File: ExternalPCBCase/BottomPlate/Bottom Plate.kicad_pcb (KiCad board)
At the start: 2 copper layers, 150 x 104.9 mm, 9 parts

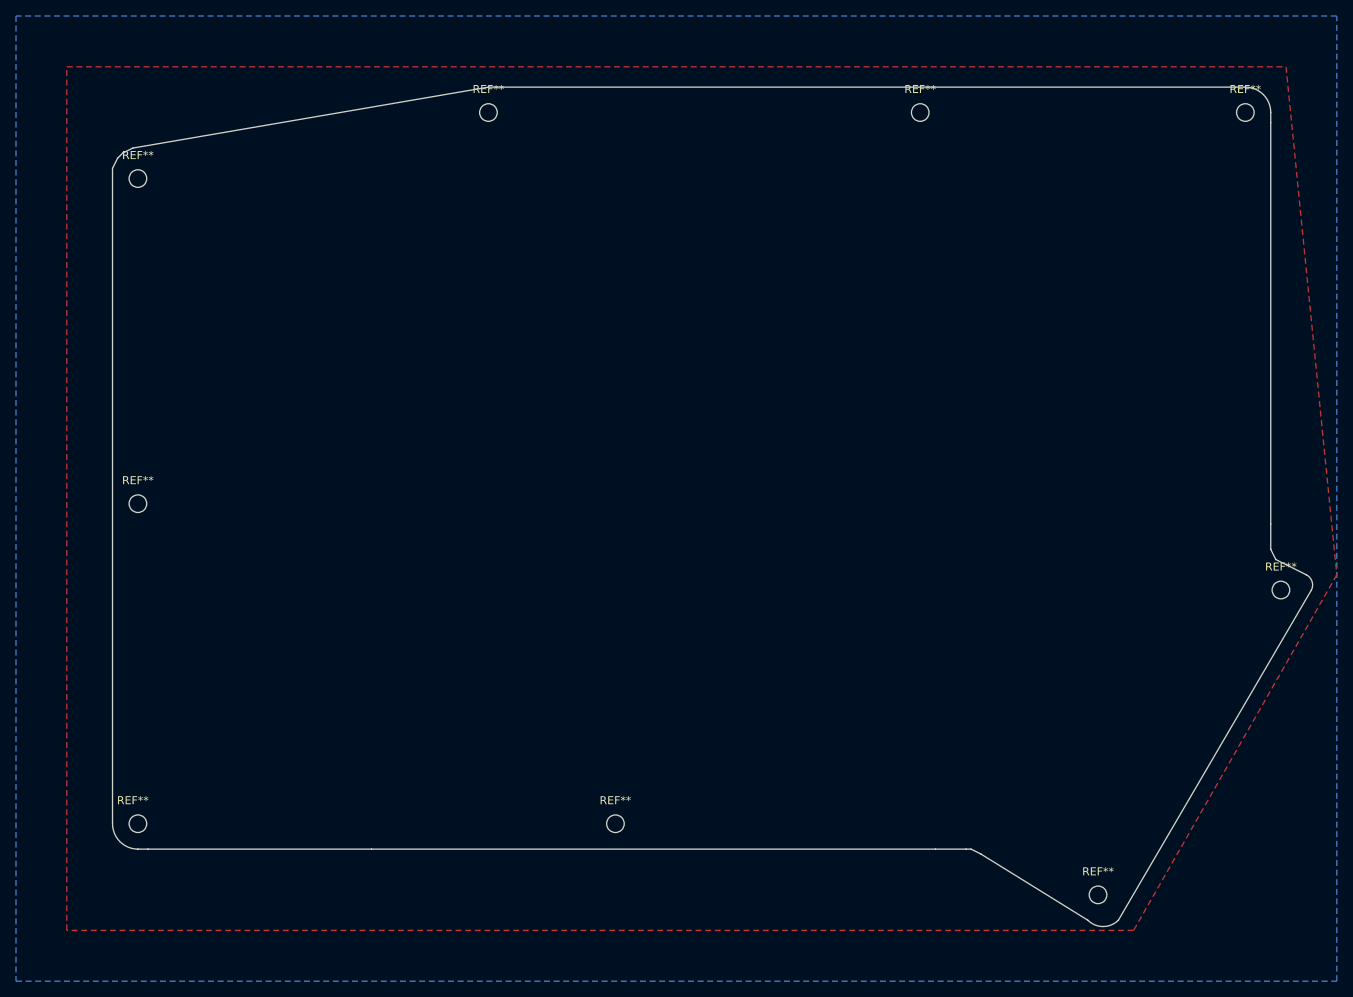
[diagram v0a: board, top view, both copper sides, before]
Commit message: Updating Internal Plates with Alps/MX Openings
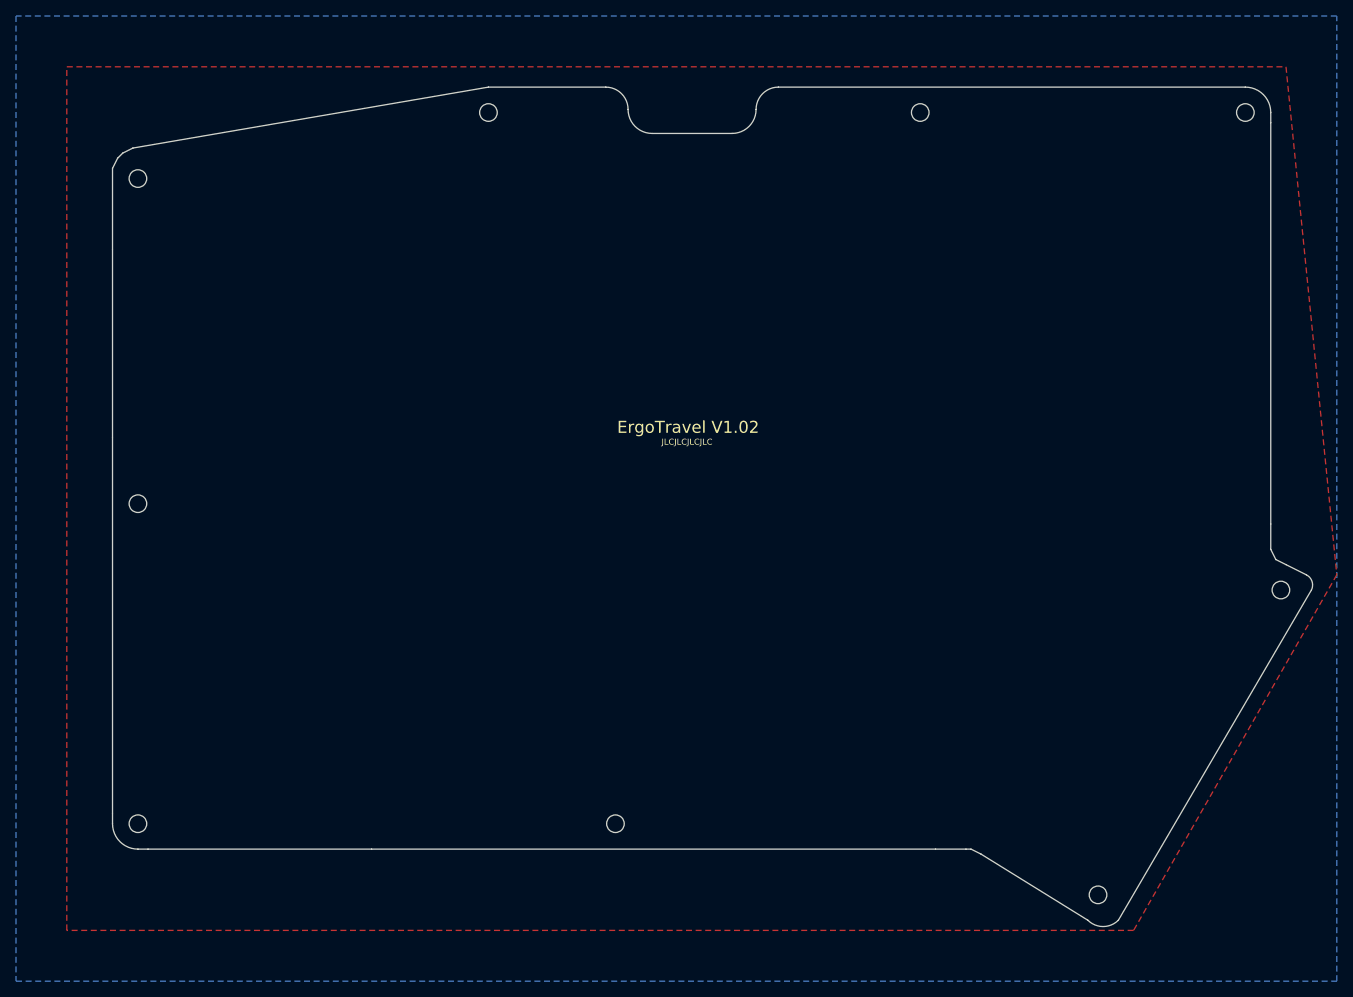
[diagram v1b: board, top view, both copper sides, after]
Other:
- outline, holes or cut-outs redrawn
- board text added: "ErgoTravel V1.02"
- board text added: "JLCJLCJLCJLC"
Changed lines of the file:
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@@
     (links 0)
     (no_connects 0)
-    (area 57.15 31.75 232.338572 152.400001)
+    (area 69.139999 40.564999 219.299904 145.644078)
     (thickness 1.6)
-    (drawings 36)
+    (drawings 45)
     (tracks 0)
     (zones 0)
@@
     (tags "mounting hole 2.2mm no annular m2 din965")
     (attr virtual)
-    (fp_text reference REF** (at 0 -2.9) (layer F.SilkS)
+    (fp_text reference REF** (at 0 -2.9) (layer F.SilkS) hide
       (effects (font (size 1 1) (thickness 0.15)))
     )
@@
     (tags "mounting hole 2.2mm no annular m2 din965")
     (attr virtual)
-    (fp_text reference REF** (at 0 -2.9) (layer F.SilkS)
+    (fp_text reference REF** (at 0 -2.9) (layer F.SilkS) hide
       (effects (font (size 1 1) (thickness 0.15)))
     )
@@
     (tags "mounting hole 2.2mm no annular m2 din965")
     (attr virtual)
-    (fp_text reference REF** (at 0 -2.9) (layer F.SilkS)
+    (fp_text reference REF** (at 0 -2.9) (layer F.SilkS) hide
       (effects (font (size 1 1) (thickness 0.15)))
     )
@@
     (tags "mounting hole 2.2mm no annular m2 din965")
     (attr virtual)
-    (fp_text reference REF** (at -0.635 -2.9) (layer F.SilkS)
+    (fp_text reference REF** (at -0.635 -2.9) (layer F.SilkS) hide
       (effects (font (size 1 1) (thickness 0.15)))
     )
@@
     (tags "mounting hole 2.2mm no annular m2 din965")
     (attr virtual)
-    (fp_text reference REF** (at 0 -2.9) (layer F.SilkS)
+    (fp_text reference REF** (at 0 -2.9) (layer F.SilkS) hide
       (effects (font (size 1 1) (thickness 0.15)))
     )
@@
     (tags "mounting hole 2.2mm no annular m2 din965")
     (attr virtual)
-    (fp_text reference REF** (at 0 -2.9) (layer F.SilkS)
+    (fp_text reference REF** (at 0 -2.9) (layer F.SilkS) hide
       (effects (font (size 1 1) (thickness 0.15)))
     )
@@
     (tags "mounting hole 2.2mm no annular m2 din965")
     (attr virtual)
-    (fp_text reference REF** (at 0 -2.9) (layer F.SilkS)
+    (fp_text reference REF** (at 0 -2.9) (layer F.SilkS) hide
       (effects (font (size 1 1) (thickness 0.15)))
     )
@@
     (tags "mounting hole 2.2mm no annular m2 din965")
     (attr virtual)
-    (fp_text reference REF** (at 0 -2.9) (layer F.SilkS)
+    (fp_text reference REF** (at 0 -2.9) (layer F.SilkS) hide
       (effects (font (size 1 1) (thickness 0.15)))
     )
@@
     (tags "mounting hole 2.2mm no annular m2 din965")
     (attr virtual)
-    (fp_text reference REF** (at 0 -2.9) (layer F.SilkS)
+    (fp_text reference REF** (at 0 -2.9) (layer F.SilkS) hide
       (effects (font (size 1 1) (thickness 0.15)))
     )
@@
     (fp_circle (center 0 0) (end 2.15 0) (layer F.CrtYd) (width 0.05))
     (pad 1 np_thru_hole circle (at 0 0) (size 2.2 2.2) (drill 2.2) (layers *.Cu *.Mask))
+  )
+  (gr_line (start 152.45 40.64) (end 210.81238 40.64) (layer Edge.Cuts) (width 0.15))
+  (gr_line (start 116.205 40.64) (end 130.87 40.64) (layer Edge.Cuts) (width 0.15))
+  (gr_arc (start 130.87 43.43) (end 133.66 43.43) (angle -90) (layer Edge.Cuts) (width 0.15))
+  (gr_arc (start 152.45 43.43) (end 149.66 43.43) (angle 90) (layer Edge.Cuts) (width 0.15))
+  (gr_arc (start 146.66 43.43) (end 149.66 43.43) (angle 90) (layer Edge.Cuts) (width 0.15))
+  (gr_arc (start 136.66 43.43) (end 136.66 46.43) (angle 90) (layer Edge.Cuts) (width 0.15))
+  (gr_line (start 136.66 46.43) (end 146.66 46.43) (layer Edge.Cuts) (width 0.15))
+  (gr_line (start 141.66 33.02) (end 141.66 53.34) (layer Dwgs.User) (width 0.2))
+  (gr_text JLCJLCJLCJLC (at 141.0208 84.9884) (layer F.SilkS)
+    (effects (font (size 0.75 0.75) (thickness 0.15)))
+  )
+  (gr_text "ErgoTravel V1.02" (at 141.1732 83.1596) (layer F.SilkS)
+    (effects (font (size 1.5 1.5) (thickness 0.3)))
   )
   (gr_line (start 70.485 48.895) (end 71.755 48.26) (layer Edge.Cuts) (width 0.15))
@@
   (gr_line (start 101.6 135.89) (end 172.085 135.89) (layer Edge.Cuts) (width 0.15))
   (gr_line (start 73.66 135.89) (end 101.6 135.89) (layer Edge.Cuts) (width 0.15))
-  (gr_line (start 116.205 40.64) (end 210.82 40.64) (layer Edge.Cuts) (width 0.15))
   (gr_line (start 71.755 48.26) (end 116.205 40.64) (layer Edge.Cuts) (width 0.15))
   (gr_line (start 69.215 84.455) (end 69.215 60.96) (layer Edge.Cuts) (width 0.15))

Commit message: last Kicad4.7 commit
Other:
- board text added: "ErgoTravel"
- board text removed: "ErgoTravel V1.02"
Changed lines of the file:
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@@
     (links 0)
     (no_connects 0)
-    (area 69.139999 40.564999 219.299904 145.644078)
+    (area 57.15 31.75 232.338572 152.400001)
     (thickness 1.6)
     (drawings 45)
@@
   (gr_line (start 136.66 46.43) (end 146.66 46.43) (layer Edge.Cuts) (width 0.15))
   (gr_line (start 141.66 33.02) (end 141.66 53.34) (layer Dwgs.User) (width 0.2))
-  (gr_text JLCJLCJLCJLC (at 141.0208 84.9884) (layer F.SilkS)
+  (gr_text JLCJLCJLCJLC (at 139.319 84.9884) (layer F.SilkS)
     (effects (font (size 0.75 0.75) (thickness 0.15)))
   )
-  (gr_text "ErgoTravel V1.02" (at 141.1732 83.1596) (layer F.SilkS)
+  (gr_text ErgoTravel (at 141.1732 83.1596) (layer F.SilkS)
     (effects (font (size 1.5 1.5) (thickness 0.3)))
   )
